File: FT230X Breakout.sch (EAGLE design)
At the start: 20 parts, among them U1 FT230XSSOP

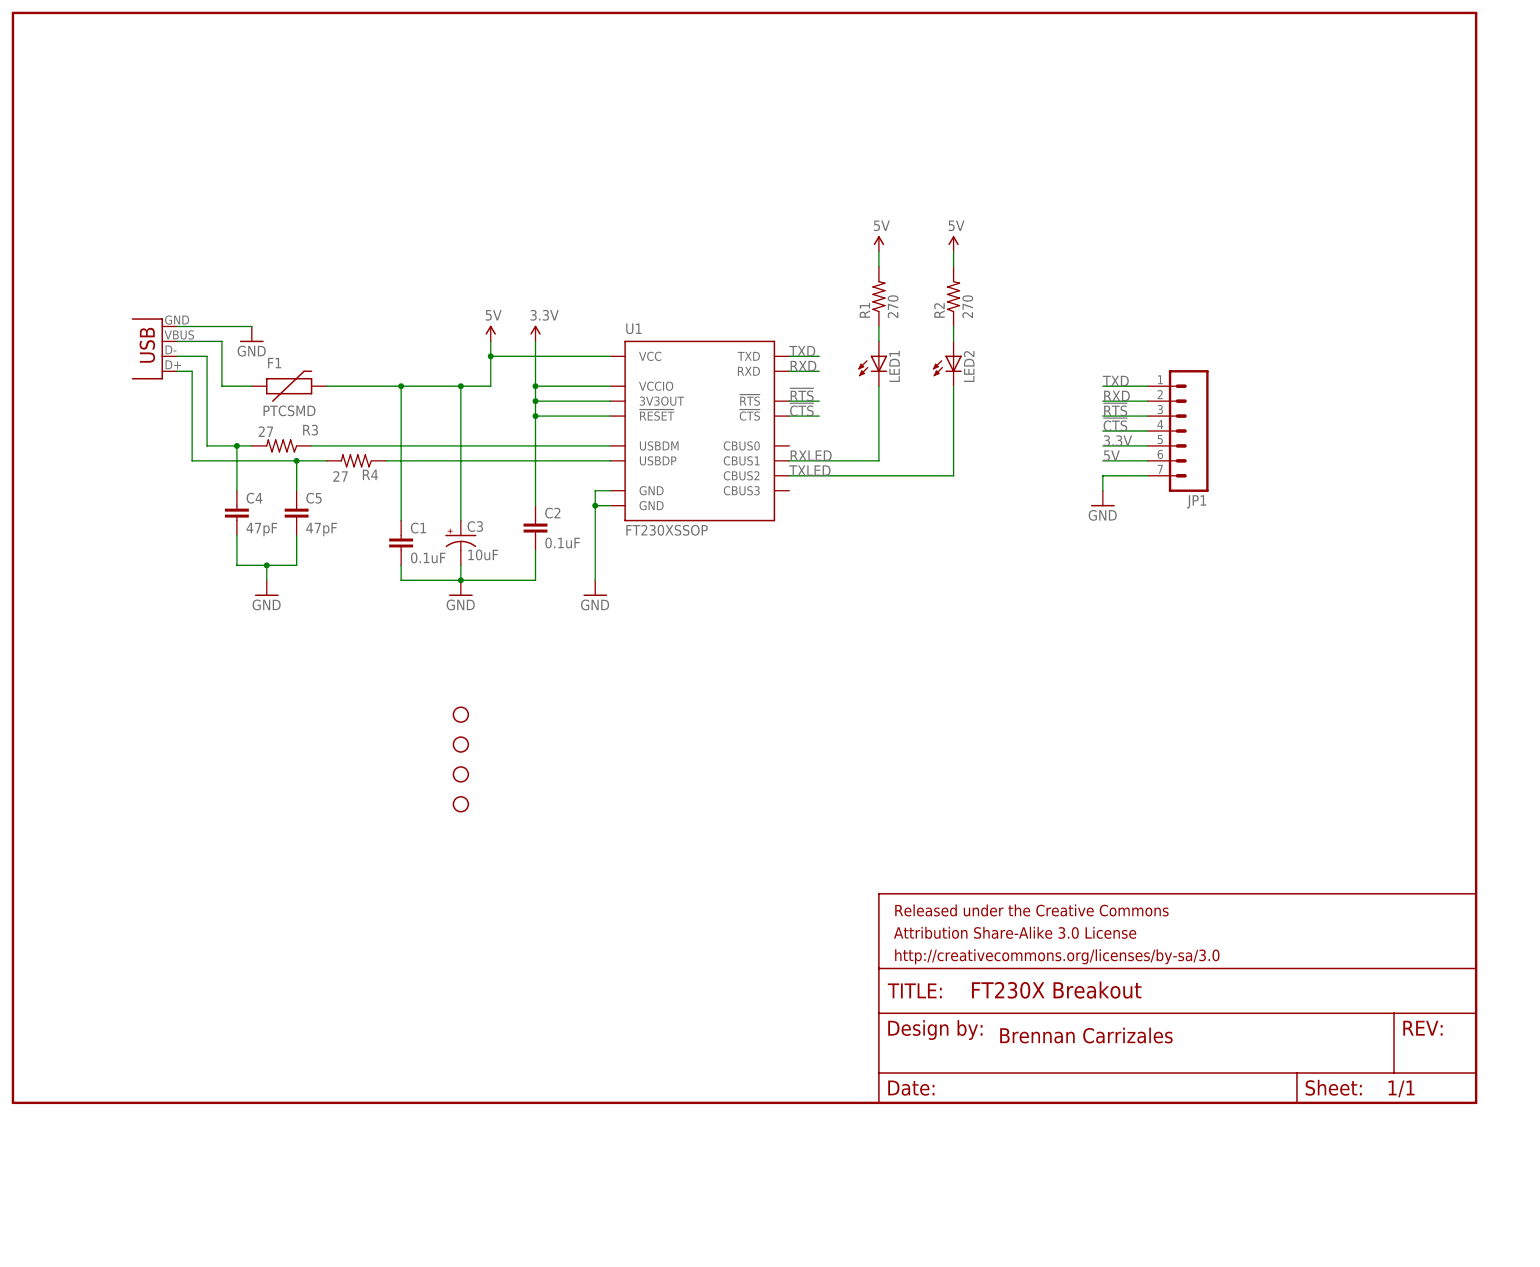
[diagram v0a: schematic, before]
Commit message: Updated Files
Updated file names. Added PDF version of schematic. Changed frame in
file.
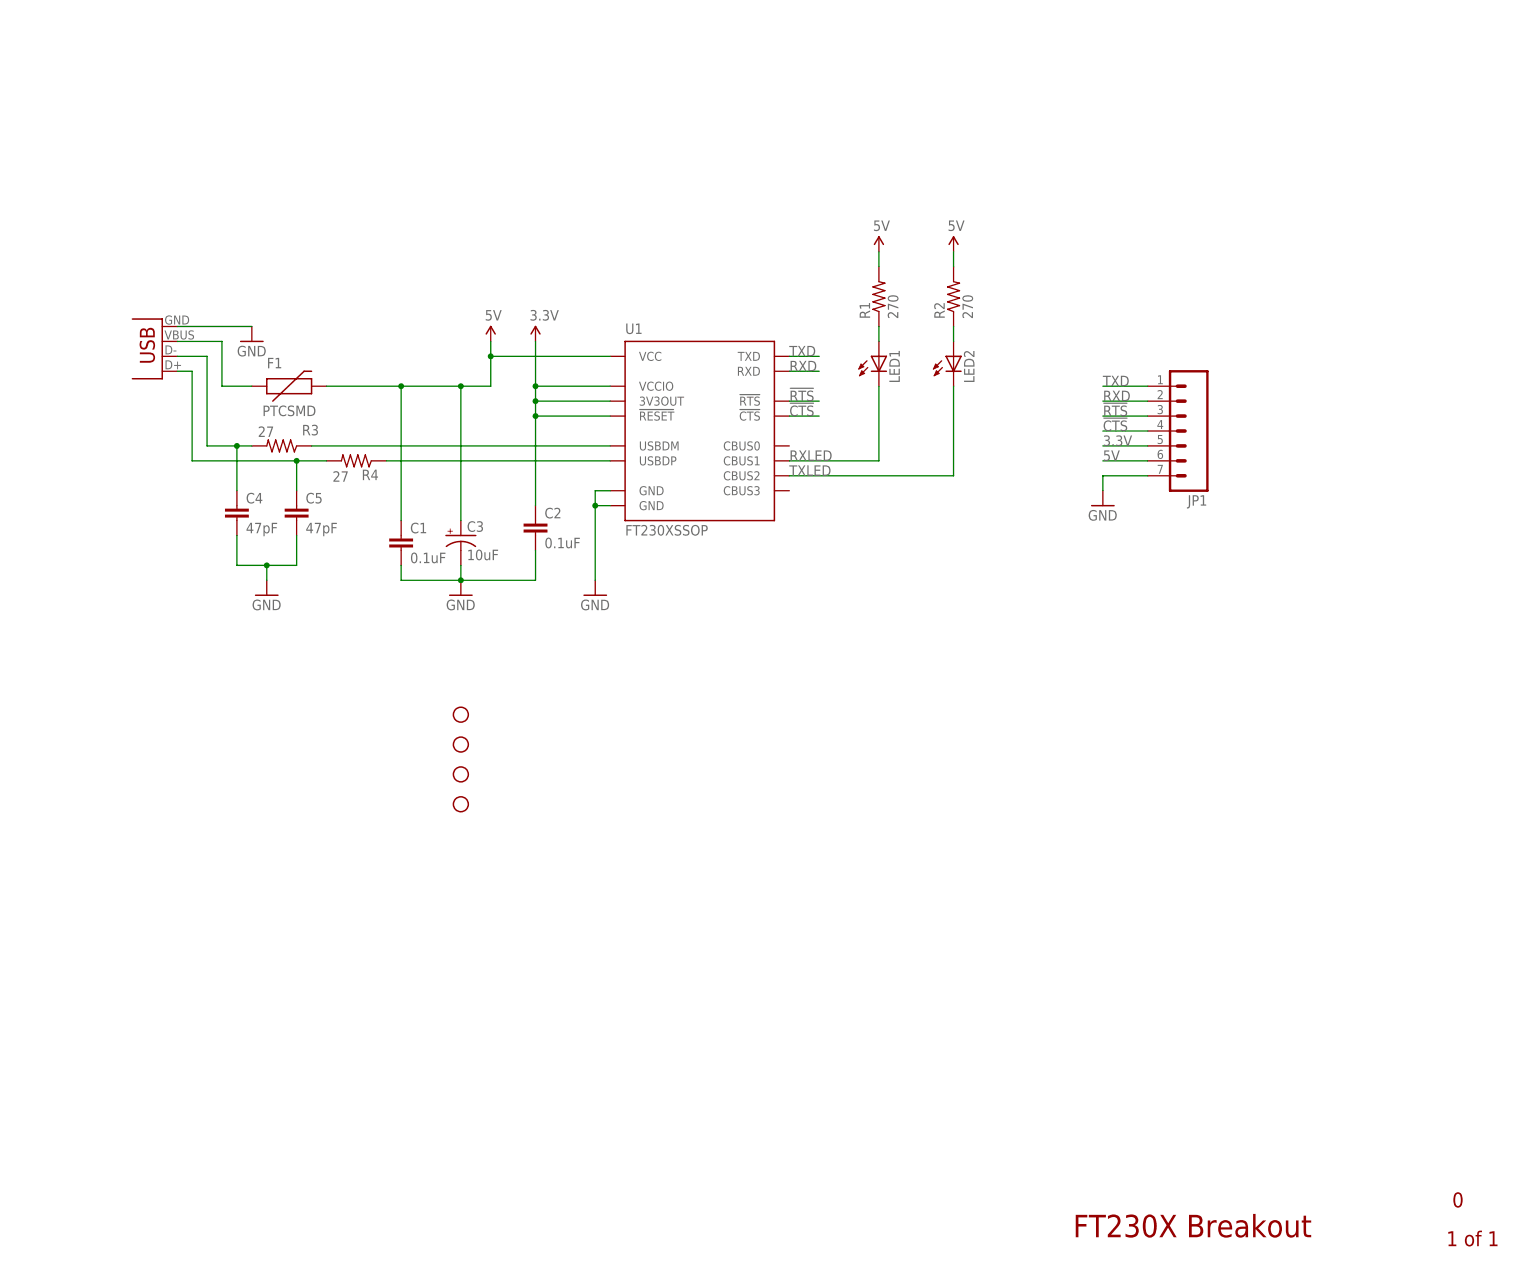
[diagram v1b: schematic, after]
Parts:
- removed FRAME1: FRAME-LETTER, SparkFun-Aesthetics:FRAME-LETTER
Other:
- note added: "0"
- note added: "1 of 1"
- note added: "FT230X Breakout"
- note removed: "Brennan Carrizales"
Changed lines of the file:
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@@
 </classes>
 <parts>
-<part name="FRAME1" library="SparkFun-Aesthetics" deviceset="FRAME-LETTER" device=""/>
 <part name="JP1" library="SparkFun-Connectors" deviceset="M07" device=""/>
 <part name="JP2" library="SparkFun-Connectors" deviceset="USB" device="SMD"/>
@@
 <part name="F1" library="SparkFun-PowerIC" deviceset="PTC" device="SMD"/>
 <part name="GND2" library="SparkFun-Aesthetics" deviceset="GND" device=""/>
+<part name="U$1" library="Misc" deviceset="FRAME_8X11" device=""/>
 </parts>
 <sheets>
 <sheet>
 <plain>
-<text x="132.08" y="-2.54" size="2.54" layer="94">Brennan Carrizales</text>
+<text x="144.78" y="-35.56" size="3.81" layer="94">FT230X Breakout</text>
+<text x="208.28" y="-37.084" size="2.54" layer="94">1 of 1</text>
+<text x="208.28" y="-30.48" size="2.54" layer="94"> 0</text>
 </plain>
 <instances>
-<instance part="FRAME1" gate="G$1" x="-35.56" y="-12.7"/>
-<instance part="FRAME1" gate="G$2" x="111.76" y="-12.7"/>
 <instance part="JP1" gate="G$1" x="162.56" y="104.14" rot="R180"/>
 <instance part="JP2" gate="G$1" x="-10.16" y="119.38" rot="R180"/>
@@
 <instance part="F1" gate="G$1" x="10.16" y="109.22"/>
 <instance part="GND2" gate="1" x="63.5" y="73.66"/>
+<instance part="U$1" gate="G$1" x="81.28" y="68.58"/>
 </instances>
 <busses>
